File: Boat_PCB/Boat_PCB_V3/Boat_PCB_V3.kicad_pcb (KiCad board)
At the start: 4 copper layers, 130.6 x 101.5 mm, 137 parts, among them J1 GPS M10-25Q, J10 Winch ESC, J11 12S HV tap (JST-VH), J12 Raspberry Pi 5 GPIO, J13 XT60 M18 ELECTRONICS, J14 XT60 M18 WINCH, J16 XT60-F WINCH ESC OUT (female), J2 Pod tether, J3 CAN stub to VESCs, J4 SHT45 external, J5 Radar stepper motor, J6 Status LED, J7 SBUS RC receiver, J8 Hull leak left, J9 Hull leak right, Q1 IPP120P04P4L-03, Q2 BSS138, Q3 BSS138, Q4 BSS138, SW1 PICO A RESET, SW2 PICO B RESET, U1 Raspberry Pi Pico 2, U10 INA228 electronics, U11 INA228 winch, U12 74AHCT1G125, U13 THVD2410, U14 Raspberry Pi Pico 2, U2 TCA9548A I2C mux, U3 TJA1051T/3 CAN xcvr, U4 BNO085, U5 ADXL375, U6 BMP390 breakout, U7 BH1750FVI-TR, U8 SHT45 internal, Y1 32.768kHz CL=12.5pF 50ppm

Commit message: feat(pcb): V3 carrier rev F, 10S power
Kyle, 2026-10-14: the full V3 runs from two 10S 10 Ah Li-ion packs in parallel, one
bus (30-42 V) for the drives, J13 (electronics) and J14 (winch), with an optional 4S
backup for the 5 V side. Rev E's electronics and winch inputs were 15-21 V domains.

Rated for 42 V:
- D3/D4 SMBJ24A -> SMBJ43A, Q1 IPP120P04P4L-03 -> SUP90P06-09L (-60 V);
- C1/C2/C26 470 uF 35 V -> 100 uF 63 V, R60 10k -> 22k.
New parts:
- U15, a Pololu D36V6F15 on the underside: +15V for the A4988 (it tops out at 35 V)
  and, through F1 and the In2 run along the top edge, the pod tether;
- D12/D13 (B360B), a diode-OR of the 10S rail and the 4S backup into the 5 V buck A2;
- J18, the 4S backup input (JST-VH), on the underside with its plug from below.
Nets: 12S_RAW/S12_ADC -> PACK_RAW/PACK_ADC, POD_VPACK -> POD_15V; new +VLOGIC,
+VBACKUP, +15V. No part moved. A placement search found the only spots that clear
every courtyard and through-hole pad, and the power runs are hand-placed.

Carrier: footprints 137 -> 141; ERC 0 -> 0, DRC 0 -> 0, unconnected 0 -> 0,
parity 0 -> 0, no exclusions. V3.1 and the pod are unchanged (all 0).

Docs follow: CLAUDE.md (terms, safety rules, pack sensing), README, Boat_PCB/CLAUDE.md
(baseline, placement, locked copper), the brief, the docs index, V3_MECHANICAL 1.1,
the scope notes of both planning files, and this week's update bullet.

Co-Authored-By: Claude Opus 5.5 <noreply@anthropic.com>
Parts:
- added D12: B360B, dreams_v3:D_SMB, B.Cu at (19.5, 31.8)
- added D13: B360B, dreams_v3:D_SMB, F.Cu at (24.6, 58.0)
- added J18: 4S backup (JST-VH), dreams_v3:JST_VH_B2P-VH_1x02_P3.96mm_Vertical, B.Cu at (33.5, 81.0)
- added U15: Pololu D36V6F15 15V 600mA, dreams_v3:Pololu_D36V6F5, B.Cu at (3.50, 35.0)
- C1, C2, C26: value 470uF 35V -> 100uF 63V
- D3, D4: value SMBJ24A -> SMBJ43A
- J11: value 12S HV tap (JST-VH) -> 10S pack tap (JST-VH)
- J13: value XT60 M18 ELECTRONICS -> XT60 10S ELECTRONICS
- J14: value XT60 M18 WINCH -> XT60 10S WINCH
- Q1: value IPP120P04P4L-03 -> SUP90P06-09L
- R60: value 10k 1% -> 22k 1%
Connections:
- net /12S_RAW renamed /PACK_RAW
- net /POD_VPACK renamed /POD_15V
- net /S12_ADC renamed /PACK_ADC
- A1 pad 8: /+VELEC -> /+15V
- A2 pad 7: /+VELEC -> /+VLOGIC
- A2 pad 8: /+VELEC -> /+VLOGIC
- C25 pad 1: /+VELEC -> /+15V
- F1 pad 1: /+VELEC -> /+15V
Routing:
- net /+15V: track 0.00 -> 178.4 mm, vias 0 -> 1
- net /+VELEC: track 190.1 -> 42.3 mm
- net /+VLOGIC: track 0.00 -> 40.7 mm
- net /+VBACKUP: track 0.00 -> 27.4 mm, vias 0 -> 2
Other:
- board text added: "10S 42V"
- board text added: "10S ELEC FUSE 5A MAX"
- board text added: "15V: POD + STEPPER"
- board text added: "4S BACKUP"
- board text added: "A2 ON BOTTOM FACE DOWN"
- board text added: "POD 15V"
- board text added: "Q1 SUP90P06-09L + INSUL HEATSINK"
- board text added: "rev F 2026-10-14"
- board text removed: "12S 50V"
- board text removed: "BUCK A2 ON BOTTOM COMPONENTS FACE DOWN"
- board text removed: "ELEC PACK FUSE 5A MAX"
- board text removed: "POD 15-21V"
- board text removed: "Q1 IPP120P04P4L-03 + INSUL HEATSINK"
- board text removed: "rev E 2026-10-13"

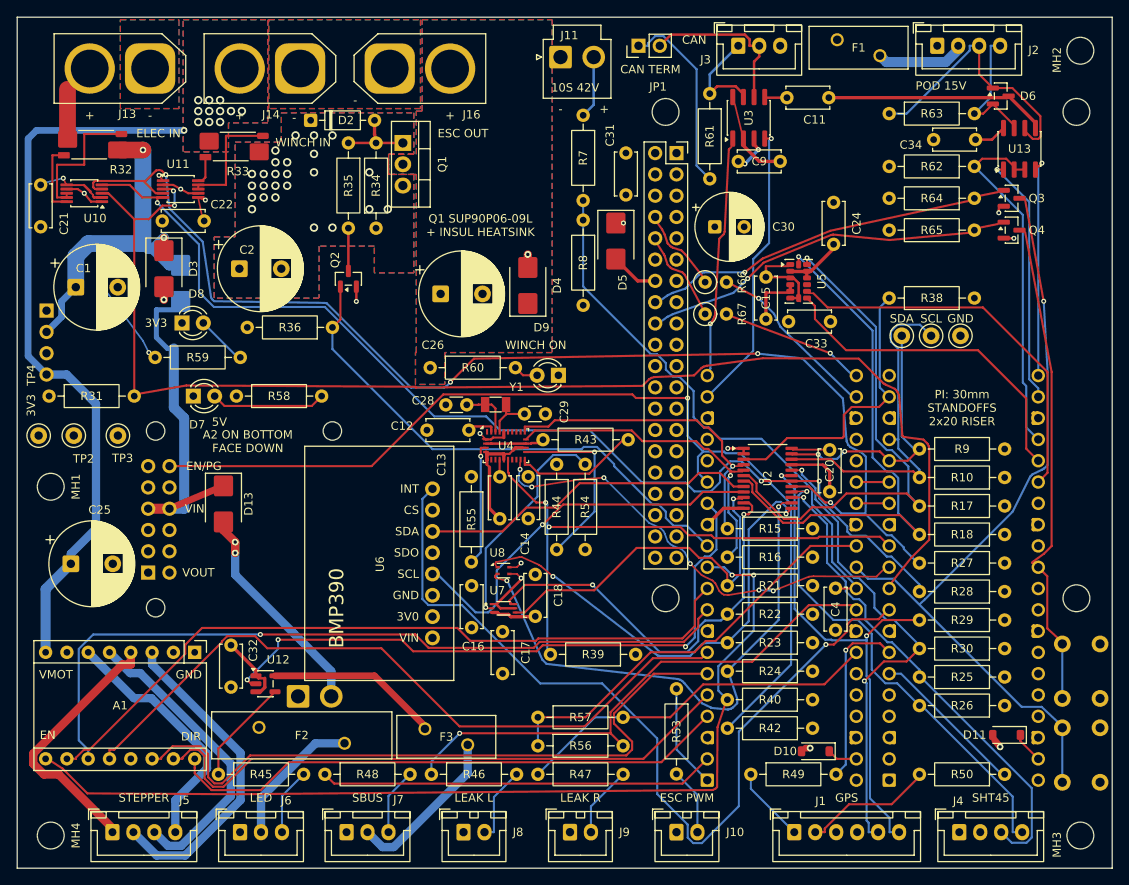
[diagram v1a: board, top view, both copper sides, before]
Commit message: feat(pcb): carrier rev F without the BMP390, condensed to 130.6 x 95.5 mm
The BMP390 breakout (U6) came off with its tracks. Its one job, a surface baseline
for the pod's pressure depth, went when depth moved to the fish-finder sonar. Mux
CH2 and Pico B GP6 are free.

With U6's area free, the bottom edge came up 6 mm. J1 (GPS) and J4 (SHT45 external)
moved into U6's old spot, because the Pi's USB jacks hang over the bottom-right
corner. The bottom connector row, its resistors and A1 moved up. J18, SW1/SW2 and
MH3/MH4 moved, and the In2 +5V zone was re-shaped. Everything that touched a moved
part was re-routed.

Carrier (Boat_PCB_V3), before -> after:
- footprints 141 -> 140
- size 130.6 x 101.5 -> 130.6 x 95.5 mm
- ERC 0 -> 0, DRC 0 -> 0, unconnected 0 -> 0, schematic parity 0 -> 0

Re-routing took tracks from 4105 to 4439 mm and vias from 119 to 141.

Docs, this week's update and the site's board renders, 3D model, poster and
callouts follow the board.

Co-Authored-By: Claude Opus 5.5 <noreply@anthropic.com>
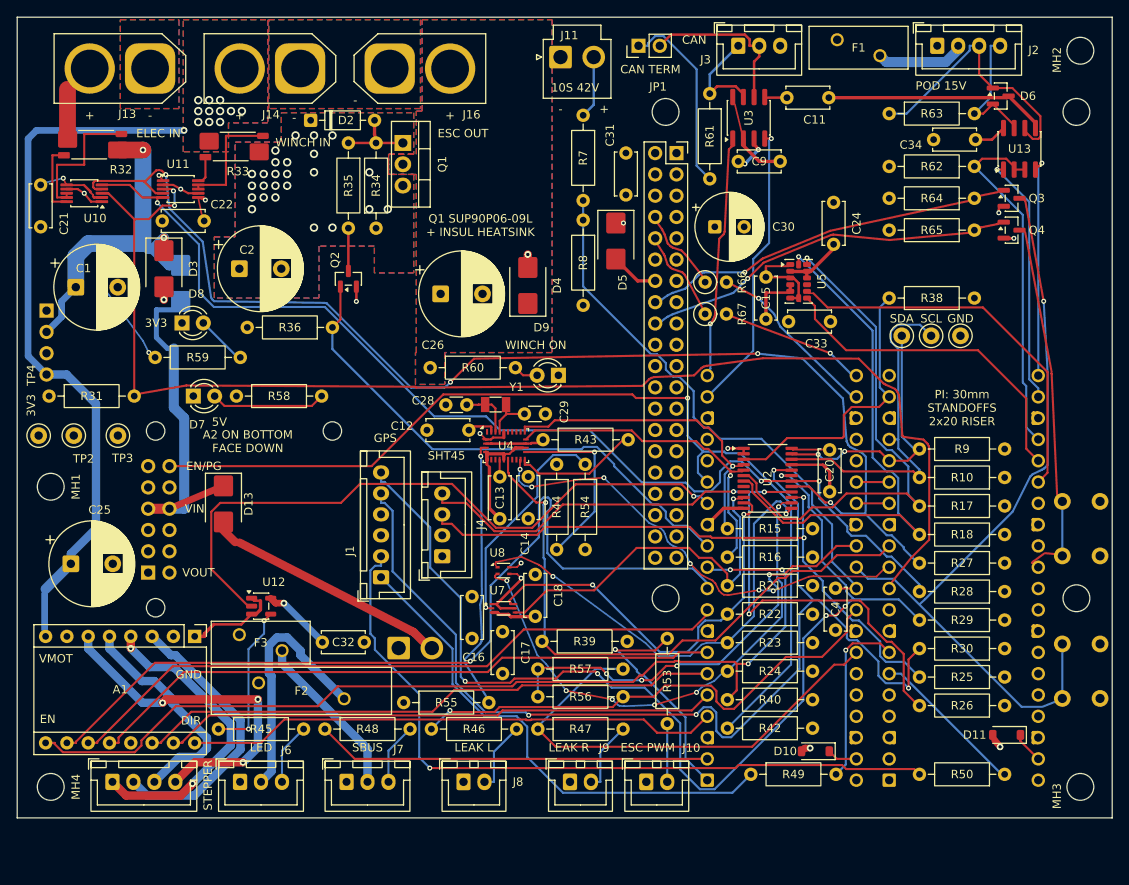
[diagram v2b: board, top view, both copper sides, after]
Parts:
- removed U6: BMP390 breakout, dreams_v3:BMP390
- moved J4 69.9 mm to (50.7, 64.3), turned to 90 degrees
- moved J1 57.9 mm to (43.4, 66.8), turned to 90 degrees
- moved R55 28.1 mm to (46.1, 81.7), turned to 0 degrees
- moved F3 24.8 mm to (26.5, 73.6)
- moved SW2 17.0 mm to (129.2, 64.2)
- moved J18 13.3 mm to (45.5, 75.2)
- moved C32 12.1 mm to (36.4, 74.5), turned to 0 degrees
- moved SW1 10.0 mm to (129.2, 81.2)
- moved U12 9.27 mm to (29.1, 70.2)
- moved J10 7.00 mm to (75.0, 91.2)
- moved R53 6.10 mm to (77.5, 74.1)
- moved J5 6.00 mm to (11.4, 91.2)
- moved J6 6.00 mm to (26.6, 91.2)
- moved J7 6.00 mm to (39.3, 91.2)
- moved J8 6.00 mm to (53.2, 91.2)
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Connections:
- U14 pad 9: /BMP_INT -> unconnected-(U14-GPIO6-Pad9)
- U2 pad 8: /CH2_SDA -> unconnected-(U2-SD2-Pad8)
- U2 pad 9: /CH2_SCL -> unconnected-(U2-SC2-Pad9)
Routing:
- net /BMP_INT: track 103.4 -> 0.00 mm, vias 1 -> 0
- net /GPS_RX_EXT: track 15.7 -> 88.1 mm, vias 0 -> 1
- net /CH7_SCL: track 56.7 -> 126.7 mm, vias 2 -> 4
- net /CH7_SDA: track 60.7 -> 127.9 mm, vias 2 -> 5
- net /GPS_TX_EXT: track 9.05 -> 60.3 mm
- net /CH2_SCL: track 47.3 -> 0.00 mm, vias 1 -> 0
- net /CH2_SDA: track 40.7 -> 0.00 mm
- net /CH5_SCL: track 57.6 -> 90.5 mm, vias 1 -> 3
- net /CH5_SDA: track 58.5 -> 76.3 mm, vias 1 -> 2
- net /PICO_B_RUN: track 57.7 -> 40.9 mm
- net /IMU_BOOTN: track 14.7 -> 31.5 mm
- net /STEP_MS1: track 88.5 -> 104.0 mm, vias 0 -> 1
- net /WINCH_PWM: track 12.4 -> 27.3 mm, vias 0 -> 1
- net /LED_5V: track 16.8 -> 29.6 mm
- net /LEAK_R: track 44.0 -> 56.8 mm
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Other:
- board size 130.6 x 101.5 mm -> 130.6 x 95.5 mm
- board text added: "rev F 2026-10-15"
- board text removed: "rev F 2026-10-14"

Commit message: feat(pcb): carrier 122.1 mm wide, every JST on an edge, A2 on top
Kyle: the strip right of the Picos held only the reset buttons, J1 (GPS) and
J4 (SHT45) sat mid-board, and the board had too much free space. Then: close
the gap where the BMP390 used to be.

- The Pi block (Pi, J12, both Picos, everything under the Pi, J3/F1/J2/MH2
  above it, SW1/SW2/MH3) moved 8.5 mm left with its own copper. Q1's heatsink
  keep-out is what stops it there.
- J1 and J4 went into the strip right of Pico B, J18 (4S backup) to the top
  side at the left edge, and J11 along the top edge next to J16 with JP1 beside
  it. J6-J9 were respaced, R7/R8 moved under the Pi, and the IMU and
  light-sensor pull-ups went into the old J1/J4 spot.
- A2 (the 5 V module) moved to the top side in the same square. Mounted
  face-down underneath, its 25 mm footprint left a patch where nothing with
  leads could go. D13 and D5 went under it, U12/F3/D7 moved, and the test
  points fill the open column by C26.
- The In2 +5V pour was widened over x 52-64 so the Pi's 5 V doesn't squeeze
  through J12's pin field, and it gained a tab for F3.
- The HV_12S net-class pattern still said /12S_RAW from rev E, so PACK_RAW had
  lost its 0.6 mm creepage rule. It's /PACK_RAW now.
- Stand-in STEP models for the D36V50F5, the A4988 carrier and the D36V6F15
  (KiCad has none), so renders show the modules instead of empty outlines.

Carrier (Boat_PCB_V3), before -> after:
- size 130.6 x 95.5 -> 122.1 x 95.5 mm (6.5% less area)
- footprints 140 -> 140; underside 8 -> 8 (A2 and J18 came up, D13 and D5 went down)
- ERC 0 -> 0, DRC 0 -> 0, unconnected 0 -> 0, schematic parity 0 -> 0
- tracks 4439 -> 4209 mm, vias 141 -> 142

Co-Authored-By: Claude Opus 5.5 <noreply@anthropic.com>
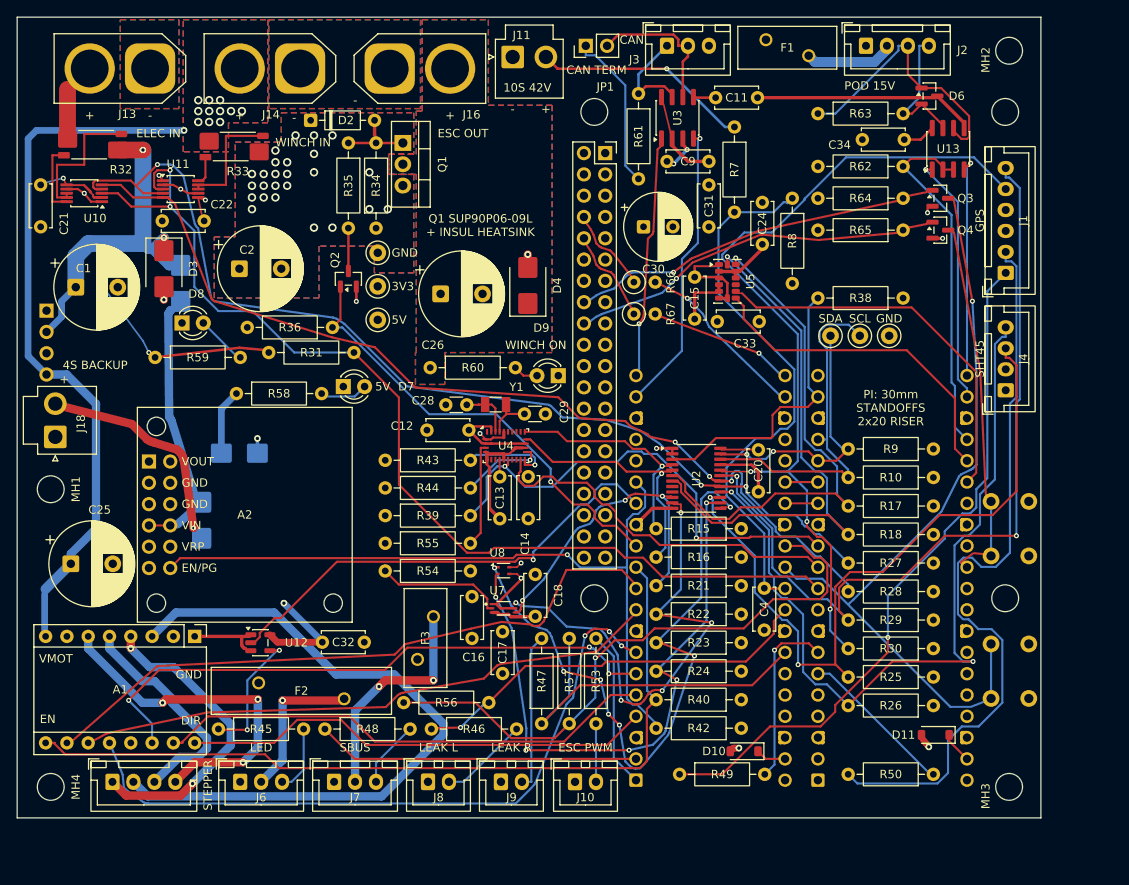
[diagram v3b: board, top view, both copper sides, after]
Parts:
- A2, J18: moved to F.Cu
- D13, D5: moved to B.Cu
- moved J1 82.9 mm to (117.9, 30.5)
- moved J4 70.1 mm to (117.9, 44.5)
- moved D5 51.5 mm to (26.5, 52.0), turned to 0 degrees
- moved J18 48.1 mm to (4.54, 50.1), turned to 90 degrees
- moved TP4 44.2 mm to (43.0, 32.1)
- moved TP2 42.3 mm to (43.0, 28.1), turned to 0 degrees
- moved TP3 33.9 mm to (43.0, 36.1)
- moved R39 32.5 mm to (43.9, 59.4), turned to 0 degrees
- moved R54 27.0 mm to (43.9, 66.0), turned to 0 degrees
- moved R31 26.7 mm to (30.0, 40.0)
- moved R8 25.1 mm to (92.4, 21.6)
- moved A2 21.6 mm to (16.6, 48.8)
- moved F3 21.5 mm to (47.7, 76.6), turned to 90 degrees
- moved R44 20.6 mm to (43.9, 56.1), turned to 0 degrees
- moved R55 19.1 mm to (43.9, 62.7)
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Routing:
- net /ST_1B: track 33.9 -> 83.5 mm
- net /PWR_GOOD: track 120.0 -> 88.6 mm
- net /INA_ALERT: track 154.5 -> 124.6 mm
- net /CH7_SDA: track 127.9 -> 99.3 mm, vias 5 -> 2
- net /CH6_SDA: track 147.5 -> 120.3 mm, vias 4 -> 3
- net /STEP_MS1: track 104.0 -> 77.7 mm, vias 1 -> 0
- net /CH4_SDA: track 54.0 -> 77.9 mm, vias 2 -> 7
- net /CH7_SCL: track 126.7 -> 103.0 mm, vias 4 -> 3
- net /LED_DIN: track 79.3 -> 56.1 mm
- net /GPS_TX_EXT: track 60.3 -> 83.0 mm, vias 0 -> 1
- net /LEAK_EXC: track 52.2 -> 71.6 mm, vias 4 -> 1
- net /IMU_BOOTN: track 31.5 -> 12.5 mm, vias 1 -> 0
- net /PACK_RAW: track 7.46 -> 25.9 mm, vias 0 -> 1
- net /STEP_EN: track 116.3 -> 98.0 mm, vias 3 -> 0
- net /IMU_RST: track 71.9 -> 57.2 mm, vias 1 -> 2
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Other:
- board size 130.6 x 95.5 mm -> 122.1 x 95.5 mm
- board text removed: "A2 ON BOTTOM FACE DOWN"
- board text removed: "EN/PG"
- board text removed: "VIN"
- board text removed: "VOUT"
